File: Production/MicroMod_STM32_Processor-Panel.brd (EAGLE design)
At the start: 132.1 x 83.1 mm, 426 parts, among them J1 MICROMOD-2222, J10 MICROMOD-2222, J2 MICROMOD-2222, J3 MICROMOD-2222, J4 MICROMOD-2222, J5 MICROMOD-2222, J6 MICROMOD-2222, J7 MICROMOD-2222, J8 MICROMOD-2222, J9 MICROMOD-2222, U1 STM32F405RGT6, U10 W25QXX128MBIT-6X5, U11 STM32F405RGT6, U12 W25QXX128MBIT-6X5, U13 STM32F405RGT6, U14 W25QXX128MBIT-6X5, U15 STM32F405RGT6, U16 W25QXX128MBIT-6X5, U17 STM32F405RGT6, U18 W25QXX128MBIT-6X5, U19 STM32F405RGT6, U2 STM32F405RGT6, U20 W25QXX128MBIT-6X5, U3 W25QXX128MBIT-6X5, U4 W25QXX128MBIT-6X5, U5 STM32F405RGT6, U6 W25QXX128MBIT-6X5, U7 STM32F405RGT6, U8 W25QXX128MBIT-6X5, U9 STM32F405RGT6, Y1 12MHz, Y10 32.768kHz, Y11 12MHz, Y12 32.768kHz, Y13 12MHz, Y14 32.768kHz, Y15 12MHz, Y16 32.768kHz, Y17 12MHz, Y18 32.768kHz, Y19 12MHz, Y2 32.768kHz, Y20 32.768kHz, Y3 12MHz, Y4 32.768kHz, Y5 12MHz, Y6 32.768kHz, Y7 12MHz, Y8 32.768kHz, Y9 12MHz

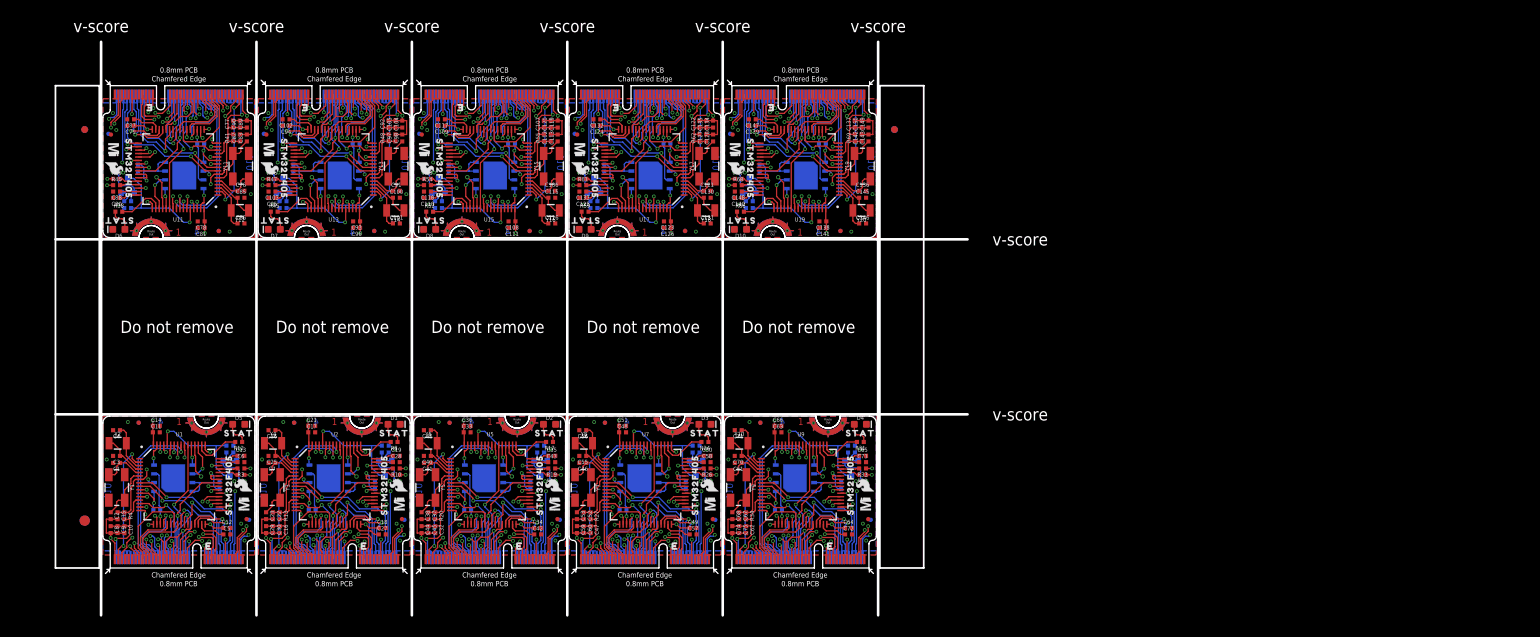
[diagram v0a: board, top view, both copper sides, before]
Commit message: Updated Panel
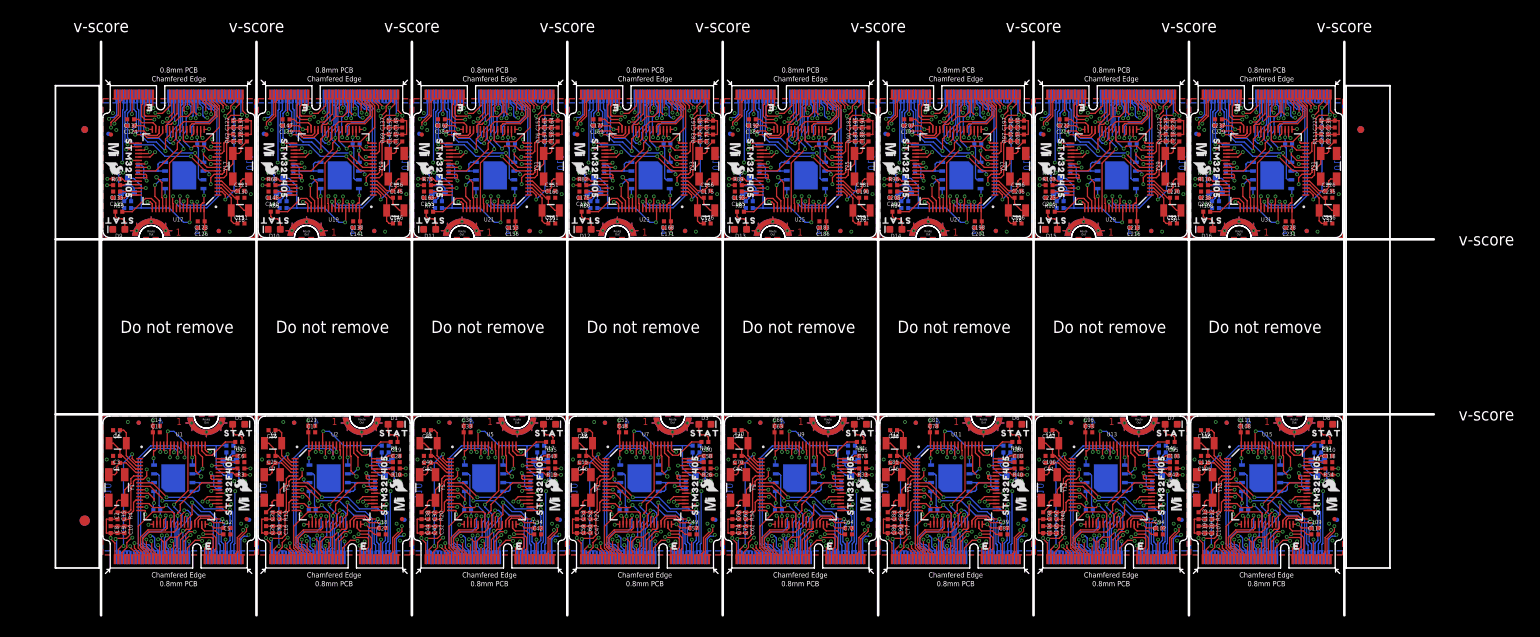
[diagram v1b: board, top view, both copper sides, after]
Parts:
- added C151, C158, C166, C173, C181, C188, C196, C203, C211, C218, C226, C233: 22pF, SparkFun-Capacitors:0402-TIGHT
- added C152, C167, C182, C197, C212, C227: 4.7uF, SparkFun-Capacitors:0402-TIGHT
- added C153, C154, C155, C156, C157, C159, C164, C168, C169, C170, C171, C172, C174, C179, C183, C184, C185, C186, C187, C189, C194, C198, C199, C200, C201, C202, C204, C209, C213, C214, C215, C216, C217, C219, C224, C228, C229, C230, C231, C232, C234, C239: 0.1uF, SparkFun-Capacitors:0402-TIGHT
- added C160, C161, C175, C176, C190, C191, C205, C206, C220, C221, C235, C236: 15pF, SparkFun-Capacitors:0402-TIGHT
- added C162, C163, C177, C178, C192, C193, C207, C208, C222, C223, C237, C238: 2.2uF, SparkFun-Capacitors:0402-TIGHT
- added C165, C180, C195, C210, C225, C240: 1.0uF, SparkFun-Capacitors:0402-TIGHT
- added D11, D12, D13, D14, D15, D16: BLUE, SparkFun-LED:LED-0603
- added FD41, FD42, FD43, FD44, FD45, FD46, FD47, FD48, FD49, FD50, FD51, FD52, FD53, FD54, FD55, FD56, FD57, FD58, FD59, FD60, FD61, FD62, FD63, FD64: FIDUCIALUFIDUCIAL, SparkFun-Aesthetics:FIDUCIAL-MICRO
- added J11, J12, J13, J14, J15, J16: MICROMOD-2222, SparkFun-MicroMod:M.2-CARD-E-22
- added LOGO21, LOGO23, LOGO25, LOGO27, LOGO29, LOGO31: OSHW-LOGOS, SparkFun-Aesthetics:OSHW-LOGO-S
- added LOGO22, LOGO24, LOGO26, LOGO28, LOGO30, LOGO32: SFE_LOGO_NAME_FLAME.1_INCH, SparkFun-Aesthetics:SFE_LOGO_NAME_FLAME_.1
- added Q11, Q12, Q13, Q14, Q15, Q16: (no value), SparkFun-DiscreteSemi:SOT23-3
- added R100, R105, R106, R107, R112, R71, R72, R77, R78, R79, R84, R85, R86, R91, R92, R93, R98, R99: 100k, SparkFun-Resistors:0402-TIGHT
- added R101, R108, R73, R80, R87, R94: 1k, SparkFun-Resistors:0402-TIGHT
- added R102, R103, R109, R110, R74, R75, R81, R82, R88, R89, R95, R96: 22, SparkFun-Resistors:0402-TIGHT
- added R104, R111, R76, R83, R90, R97: 5.1k, SparkFun-Resistors:0402-TIGHT
- added U$100, U$107, U$72, U$79, U$86, U$93: (no value), output:STM320
- added U$101, U$108, U$73, U$80, U$87, U$94: (no value), SparkFun-MicroMod:MICROMOD_MI_LOGO_.35
- added U$102, U$109, U$74, U$81, U$88, U$95: (no value), output:STM32F4050
- added U$103, U$110, U$75, U$82, U$89, U$96: (no value), SparkFun-MicroMod:MICROMOD_LOGO_.3
- added U$104, U$111, U$76, U$83, U$90, U$97: (no value), SparkFun-Aesthetics:SFE_LOGO_FLAME_.1
- added U$105, U$112, U$77, U$84, U$91, U$98: (no value), SparkFun-Aesthetics:PRODUCTION_INSTRUCTIONS
- added U$106, U$71, U$78, U$85, U$92, U$99: (no value), output:STAT0
- added U21, U23, U25, U27, U29, U31: STM32F405RGT6, STM32_Temp:TQFP64
- added U22, U24, U26, U28, U30, U32: W25QXX128MBIT-6X5, SparkFun-MicroMod:WSON-8-6X5
- added Y21, Y23, Y25, Y27, Y29, Y31: 12MHz, SparkFun-Clocks:CRYSTAL-SMD-5X3.2-4PAD
- added Y22, Y24, Y26, Y28, Y30, Y32: 32.768kHz, SparkFun-Clocks:CRYSTAL-SMD-3.2X1.5MM
- moved U$42 166.9 mm to (149.5, 49.0), turned to 0 degrees
- moved U$49 166.9 mm to (172.0, 49.0), turned to 0 degrees
- moved U$56 166.9 mm to (194.6, 49.0), turned to 0 degrees
- moved FD23 144.2 mm to (133.7, 6.97), turned to 0 degrees
- moved FD27 144.2 mm to (156.2, 6.97), turned to 0 degrees
- moved FD31 144.2 mm to (178.7, 6.97), turned to 0 degrees
- moved FD25 143.4 mm to (155.9, 7.08), turned to 0 degrees
- moved FD29 143.4 mm to (178.4, 7.08), turned to 0 degrees
- moved FD21 143.4 mm to (133.4, 7.08), turned to 0 degrees
- moved U$45 141.1 mm to (155.5, 9.23), turned to 90 degrees
- moved U$52 141.1 mm to (178.0, 9.23), turned to 90 degrees
- moved U$38 141.1 mm to (133.0, 9.23), turned to 90 degrees
- moved C87 140.0 mm to (130.5, 4.87), turned to 0 degrees
- moved C102 140.0 mm to (153.0, 4.87), turned to 0 degrees
- moved C117 140.0 mm to (175.5, 4.87), turned to 0 degrees
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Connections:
- new net !BOOT10: J11.11, Q11.1, R77.1
- new net !BOOT11: J12.11, Q12.1, R84.1
- new net !BOOT12: J13.11, Q13.1, R91.1
- new net !BOOT13: J14.11, Q14.1, R98.1
- new net !BOOT14: J15.11, Q15.1, R105.1
- new net !BOOT15: J16.11, Q16.1, R112.1
- new net !CS10: J11.55, U21.24
- new net !CS11: J12.55, U23.24
- new net !CS12: J13.55, U25.24
- new net !CS13: J14.55, U27.24
- new net !CS14: J15.55, U29.24
- new net !CS15: J16.55, U31.24
- new net !INT10: J11.16, U21.27
- new net !INT11: J12.16, U23.27
- new net !INT12: J13.16, U25.27
- new net !INT13: J14.16, U27.27
- new net !INT14: J15.16, U29.27
- new net !INT15: J16.16, U31.27
- new net !RESET10: C157.1, J11.6, R76.1, U21.7
- new net !RESET11: C172.1, J12.6, R83.1, U23.7
- new net !RESET12: C187.1, J13.6, R90.1, U25.7
- new net !RESET13: C202.1, J14.6, R97.1, U27.7
- new net !RESET14: C217.1, J15.6, R104.1, U29.7
- new net !RESET15: C232.1, J16.6, R111.1, U31.7
- new net 3.3V10: C152.1, C153.1, C154.1, C155.1, C156.1, C159.1, C164.1, C165.1, J11.2, J11.74, Q11.2, R72.2, R76.2, R77.2, U21.13, U21.19, U21.32, U21.42, U21.43, U21.48, U21.64, U22.3, U22.7, U22.8
- new net 3.3V11: C167.1, C168.1, C169.1, C170.1, C171.1, C174.1, C179.1, C180.1, J12.2, J12.74, Q12.2, R79.2, R83.2, R84.2, U23.13, U23.19, U23.32, U23.42, U23.43, U23.48, U23.64, U24.3, U24.7, U24.8
- new net 3.3V12: C182.1, C183.1, C184.1, C185.1, C186.1, C189.1, C194.1, C195.1, J13.2, J13.74, Q13.2, R86.2, R90.2, R91.2, U25.13, U25.19, U25.32, U25.42, U25.43, U25.48, U25.64, U26.3, U26.7, U26.8
- new net 3.3V13: C197.1, C198.1, C199.1, C200.1, C201.1, C204.1, C209.1, C210.1, J14.2, J14.74, Q14.2, R93.2, R97.2, R98.2, U27.13, U27.19, U27.32, U27.42, U27.43, U27.48, U27.64, U28.3, U28.7, U28.8
- new net 3.3V14: C212.1, C213.1, C214.1, C215.1, C216.1, C219.1, C224.1, C225.1, J15.2, J15.74, Q15.2, R100.2, R104.2, R105.2, U29.13, U29.19, U29.32, U29.42, U29.43, U29.48, U29.64, U30.3, U30.7, U30.8
- new net 3.3V15: C227.1, C228.1, C229.1, C230.1, C231.1, C234.1, C239.1, C240.1, J16.2, J16.74, Q16.2, R107.2, R111.2, R112.2, U31.13, U31.19, U31.32, U31.42, U31.43, U31.48, U31.64, U32.3, U32.7, U32.8
- new net A20: J11.34, U21.25
- new net A21: J11.38, U21.26
- new net A22: J12.34, U23.25
- new net A23: J12.38, U23.26
- new net A24: J13.34, U25.25
- new net A25: J13.38, U25.26
- new net A26: J14.34, U27.25
- new net A27: J14.38, U27.26
- new net A28: J15.34, U29.25
- new net A29: J15.38, U29.26
- new net A30: J16.34, U31.25
- new net A31: J16.38, U31.26
- new net AUD_BCLK10: J11.50, U21.55
- new net AUD_BCLK11: J12.50, U23.55
- new net AUD_BCLK12: J13.50, U25.55
- new net AUD_BCLK13: J14.50, U27.55
- new net AUD_BCLK14: J15.50, U29.55
- new net AUD_BCLK15: J16.50, U31.55
- new net AUD_IN10: J11.54, U21.57
- new net AUD_IN11: J12.54, U23.57
- new net AUD_IN12: J13.54, U25.57
- new net AUD_IN13: J14.54, U27.57
- new net AUD_IN14: J15.54, U29.57
- new net AUD_IN15: J16.54, U31.57
- new net AUD_LRCLK10: J11.52, U21.20
- new net AUD_LRCLK11: J12.52, U23.20
- new net AUD_LRCLK12: J13.52, U25.20
- new net AUD_LRCLK13: J14.52, U27.20
- new net AUD_LRCLK14: J15.52, U29.20
- new net AUD_LRCLK15: J16.52, U31.20
- new net AUD_OUT10: J11.56, U21.56
- new net AUD_OUT11: J12.56, U23.56
- new net AUD_OUT12: J13.56, U25.56
- new net AUD_OUT13: J14.56, U27.56
- new net AUD_OUT14: J15.56, U29.56
- new net AUD_OUT15: J16.56, U31.56
- new net BATT_VIN10: J11.49, U21.15
- new net BATT_VIN11: J12.49, U23.15
- new net BATT_VIN12: J13.49, U25.15
- new net BATT_VIN13: J14.49, U27.15
- new net BATT_VIN14: J15.49, U29.15
- new net BATT_VIN15: J16.49, U31.15
- new net BOOT10: Q11.3, R71.2, U21.60
- new net BOOT11: Q12.3, R78.2, U23.60
- new net BOOT12: Q13.3, R85.2, U25.60
- new net BOOT13: Q14.3, R92.2, U27.60
- new net BOOT14: Q15.3, R99.2, U29.60
- new net BOOT15: Q16.3, R106.2, U31.60
- new net CAN_RX10: J11.41, U21.61
- new net CAN_RX11: J12.41, U23.61
- new net CAN_RX12: J13.41, U25.61
- new net CAN_RX13: J14.41, U27.61
- new net CAN_RX14: J15.41, U29.61
- new net CAN_RX15: J16.41, U31.61
- new net CAN_TX10: J11.43, U21.62
- new net CAN_TX11: J12.43, U23.62
- new net CAN_TX12: J13.43, U25.62
- new net CAN_TX13: J14.43, U27.62
- new net CAN_TX14: J15.43, U29.62
- new net CAN_TX15: J16.43, U31.62
- new net CIPO10: J11.61, U21.22
- new net CIPO11: J12.61, U23.22
- new net CIPO12: J13.61, U25.22
- new net CIPO13: J14.61, U27.22
- new net CIPO14: J15.61, U29.22
- new net CIPO15: J16.61, U31.22
- new net COPI10: J11.59, U21.23
- new net COPI11: J12.59, U23.23
- new net COPI12: J13.59, U25.23
- new net COPI13: J14.59, U27.23
- new net COPI14: J15.59, U29.23
- new net COPI15: J16.59, U31.23
- new net D+10: J11.3, R75.1
- new net D+11: J12.3, R82.1
- new net D+12: J13.3, R89.1
- new net D+13: J14.3, R96.1
- new net D+14: J15.3, R103.1
- new net D+15: J16.3, R110.1
- new net D-10: J11.5, R74.1
- new net D-11: J12.5, R81.1
- new net D-12: J13.5, R88.1
- new net D-13: J14.5, R95.1
- new net D-14: J15.5, R102.1
- new net D-15: J16.5, R109.1
- new net D20: J11.10, U21.8
- new net D21: J11.18, U21.9
- new net D22: J12.10, U23.8
- new net D23: J12.18, U23.9
- new net D24: J13.10, U25.8
- new net D25: J13.18, U25.9
- new net D26: J14.10, U27.8
- new net D27: J14.18, U27.9
- new net D28: J15.10, U29.8
- new net D29: J15.18, U29.9
- new net D30: J16.10, U31.8
- new net D31: J16.18, U31.9
- new net FLASH_!CS10: R72.1, U21.11, U22.1
- new net FLASH_!CS11: R79.1, U23.11, U24.1
- new net FLASH_!CS12: R86.1, U25.11, U26.1
- new net FLASH_!CS13: R93.1, U27.11, U28.1
- new net FLASH_!CS14: R100.1, U29.11, U30.1
- new net FLASH_!CS15: R107.1, U31.11, U32.1
- new net FLASH_SCK10: U21.51, U22.6
- new net FLASH_SCK11: U23.51, U24.6
- new net FLASH_SCK12: U25.51, U26.6
- new net FLASH_SCK13: U27.51, U28.6
- new net FLASH_SCK14: U29.51, U30.6
- new net FLASH_SCK15: U31.51, U32.6
- new net FLASH_SDI10: U21.53, U22.5
- new net FLASH_SDI11: U23.53, U24.5
- new net FLASH_SDI12: U25.53, U26.5
- new net FLASH_SDI13: U27.53, U28.5
- new net FLASH_SDI14: U29.53, U30.5
- new net FLASH_SDI15: U31.53, U32.5
- new net FLASH_SDO10: U21.52, U22.2
- new net FLASH_SDO11: U23.52, U24.2
- new net FLASH_SDO12: U25.52, U26.2
- new net FLASH_SDO13: U27.52, U28.2
- new net FLASH_SDO14: U29.52, U30.2
- new net FLASH_SDO15: U31.52, U32.2
- new net G100: J15.46, U29.39
- new net G101: J15.48, U29.40
- new net G102: J15.40, U29.54
- new net G103: J15.42, U29.41
- new net G104: J15.44, U29.14
- new net G105: J16.73, U31.2
- new net G106: J16.71, U31.10
- new net G107: J16.46, U31.39
- new net G108: J16.48, U31.40
- new net G109: J16.40, U31.54
- new net G110: J16.42, U31.41
- new net G111: J16.44, U31.14
- new net G70: J11.73, U21.2
- new net G71: J11.71, U21.10
- new net G72: J11.46, U21.39
- new net G73: J11.48, U21.40
- new net G74: J11.40, U21.54
- new net G75: J11.42, U21.41
- new net G76: J11.44, U21.14
- new net G77: J12.73, U23.2
- new net G78: J12.71, U23.10
- new net G79: J12.46, U23.39
- new net G80: J12.48, U23.40
- new net G81: J12.40, U23.54
- new net G82: J12.42, U23.41
- new net G83: J12.44, U23.14
- new net G84: J13.73, U25.2
- new net G85: J13.71, U25.10
- new net G86: J13.46, U25.39
- new net G87: J13.48, U25.40
- new net G88: J13.40, U25.54
- new net G89: J13.42, U25.41
- new net G90: J13.44, U25.14
- new net G91: J14.73, U27.2
- new net G92: J14.71, U27.10
- new net G93: J14.46, U27.39
- new net G94: J14.48, U27.40
- new net G95: J14.40, U27.54
- new net G96: J14.42, U27.41
- new net G97: J14.44, U27.14
- new net G98: J15.73, U29.2
- new net G99: J15.71, U29.10
- new net GND10: C151.2, C152.2, C153.2, C154.2, C155.2, C156.2, C157.2, C158.2, C159.2, C160.2, C161.2, C162.2, C163.2, C164.2, C165.2, D11.C, J11.1, J11.33, J11.36, J11.39, J11.45, J11.7, J11.75, J11.GND1, J11.GND2, J11.GND3, R71.1, U21.12, U21.18, U21.28, U21.63, U22.4
- new net GND11: C166.2, C167.2, C168.2, C169.2, C170.2, C171.2, C172.2, C173.2, C174.2, C175.2, C176.2, C177.2, C178.2, C179.2, C180.2, D12.C, J12.1, J12.33, J12.36, J12.39, J12.45, J12.7, J12.75, J12.GND1, J12.GND2, J12.GND3, R78.1, U23.12, U23.18, U23.28, U23.63, U24.4
- new net GND12: C181.2, C182.2, C183.2, C184.2, C185.2, C186.2, C187.2, C188.2, C189.2, C190.2, C191.2, C192.2, C193.2, C194.2, C195.2, D13.C, J13.1, J13.33, J13.36, J13.39, J13.45, J13.7, J13.75, J13.GND1, J13.GND2, J13.GND3, R85.1, U25.12, U25.18, U25.28, U25.63, U26.4
- new net GND13: C196.2, C197.2, C198.2, C199.2, C200.2, C201.2, C202.2, C203.2, C204.2, C205.2, C206.2, C207.2, C208.2, C209.2, C210.2, D14.C, J14.1, J14.33, J14.36, J14.39, J14.45, J14.7, J14.75, J14.GND1, J14.GND2, J14.GND3, R92.1, U27.12, U27.18, U27.28, U27.63, U28.4
- new net GND14: C211.2, C212.2, C213.2, C214.2, C215.2, C216.2, C217.2, C218.2, C219.2, C220.2, C221.2, C222.2, C223.2, C224.2, C225.2, D15.C, J15.1, J15.33, J15.36, J15.39, J15.45, J15.7, J15.75, J15.GND1, J15.GND2, J15.GND3, R99.1, U29.12, U29.18, U29.28, U29.63, U30.4
- new net GND15: C226.2, C227.2, C228.2, C229.2, C230.2, C231.2, C232.2, C233.2, C234.2, C235.2, C236.2, C237.2, C238.2, C239.2, C240.2, D16.C, J16.1, J16.33, J16.36, J16.39, J16.45, J16.7, J16.75, J16.GND1, J16.GND2, J16.GND3, R106.1, U31.12, U31.18, U31.28, U31.63, U32.4
- new net HOST_D+10: J11.35, U21.36
- new net HOST_D+11: J12.35, U23.36
- new net HOST_D+12: J13.35, U25.36
- new net HOST_D+13: J14.35, U27.36
- new net HOST_D+14: J15.35, U29.36
- new net HOST_D+15: J16.35, U31.36
- new net HOST_D-10: J11.37, U21.35
- new net HOST_D-11: J12.37, U23.35
- new net HOST_D-12: J13.37, U25.35
- new net HOST_D-13: J14.37, U27.35
- new net HOST_D-14: J15.37, U29.35
- new net HOST_D-15: J16.37, U31.35
- new net HOST_ID10: J11.8, U21.33
- new net HOST_ID11: J12.8, U23.33
- new net HOST_ID12: J13.8, U25.33
- new net HOST_ID13: J14.8, U27.33
- new net HOST_ID14: J15.8, U29.33
- new net HOST_ID15: J16.8, U31.33
- new net HOST_VBUS10: J11.63, U21.34
- new net HOST_VBUS11: J12.63, U23.34
- new net HOST_VBUS12: J13.63, U25.34
- new net HOST_VBUS13: J14.63, U27.34
- new net HOST_VBUS14: J15.63, U29.34
- new net HOST_VBUS15: J16.63, U31.34
- new net N$100: C176.1, U23.3, Y24.P$2
- new net N$101: C175.1, U23.4, Y24.P$1
- new net N$102: C173.1, U23.6, Y23.3
- new net N$103: C166.1, U23.5, Y23.1
- new net N$104: C178.1, U23.47
- new net N$105: C177.1, U23.31
- new net N$106: D12.A, R80.1
- new net N$107: R81.2, U23.44
- new net N$108: R82.2, U23.45
- new net N$109: C191.1, U25.3, Y26.P$2
- new net N$110: C190.1, U25.4, Y26.P$1
- new net N$111: C188.1, U25.6, Y25.3
- new net N$112: C181.1, U25.5, Y25.1
- new net N$113: C193.1, U25.47
- new net N$114: C192.1, U25.31
- new net N$115: D13.A, R87.1
- new net N$116: R88.2, U25.44
- new net N$117: R89.2, U25.45
- new net N$118: C206.1, U27.3, Y28.P$2
- new net N$119: C205.1, U27.4, Y28.P$1
- new net N$120: C203.1, U27.6, Y27.3
- new net N$121: C196.1, U27.5, Y27.1
- new net N$122: C208.1, U27.47
- new net N$123: C207.1, U27.31
- new net N$124: D14.A, R94.1
- new net N$125: R95.2, U27.44
- new net N$126: R96.2, U27.45
- new net N$127: C221.1, U29.3, Y30.P$2
- new net N$128: C220.1, U29.4, Y30.P$1
- new net N$129: C218.1, U29.6, Y29.3
- new net N$130: C211.1, U29.5, Y29.1
- new net N$131: C223.1, U29.47
- new net N$132: C222.1, U29.31
- new net N$133: D15.A, R101.1
- new net N$134: R102.2, U29.44
- new net N$135: R103.2, U29.45
- new net N$136: C236.1, U31.3, Y32.P$2
- new net N$137: C235.1, U31.4, Y32.P$1
- new net N$138: C233.1, U31.6, Y31.3
- new net N$139: C226.1, U31.5, Y31.1
- new net N$140: C238.1, U31.47
- new net N$141: C237.1, U31.31
- new net N$142: D16.A, R108.1
- new net N$143: R109.2, U31.44
- new net N$144: R110.2, U31.45
- new net N$91: C161.1, U21.3, Y22.P$2
- new net N$92: C160.1, U21.4, Y22.P$1
- new net N$93: C158.1, U21.6, Y21.3
- new net N$94: C151.1, U21.5, Y21.1
- new net N$95: C163.1, U21.47
- new net N$96: C162.1, U21.31
- new net N$97: D11.A, R73.1
- new net N$98: R74.2, U21.44
- new net N$99: R75.2, U21.45
- new net PWM20: J11.32, U21.37
- new net PWM21: J11.47, U21.38
- new net PWM22: J12.32, U23.37
- new net PWM23: J12.47, U23.38
- new net PWM24: J13.32, U25.37
- new net PWM25: J13.47, U25.38
- new net PWM26: J14.32, U27.37
- new net PWM27: J14.47, U27.38
- new net PWM28: J15.32, U29.37
- new net PWM29: J15.47, U29.38
- new net PWM30: J16.32, U31.37
- new net PWM31: J16.47, U31.38
- new net RX11: J11.19, U21.17
- new net RX12: J12.19, U23.17
- new net RX13: J13.19, U25.17
- new net RX14: J14.19, U27.17
- new net RX15: J15.19, U29.17
- new net RX16: J16.19, U31.17
- new net SCK10: J11.57, U21.21
- new net SCK11: J12.57, U23.21
- new net SCK12: J13.57, U25.21
- new net SCK13: J14.57, U27.21
- new net SCK14: J15.57, U29.21
- new net SCK15: J16.57, U31.21
- new net SCL20: J11.14, U21.29
- new net SCL21: J11.53, U21.58
- new net SCL22: J12.14, U23.29
- new net SCL23: J12.53, U23.58
- new net SCL24: J13.14, U25.29
- new net SCL25: J13.53, U25.58
- new net SCL26: J14.14, U27.29
- new net SCL27: J14.53, U27.58
- new net SCL28: J15.14, U29.29
- new net SCL29: J15.53, U29.58
- new net SCL30: J16.14, U31.29
- new net SCL31: J16.53, U31.58
- new net SDA20: J11.12, U21.30
- new net SDA21: J11.51, U21.59
- new net SDA22: J12.12, U23.30
- new net SDA23: J12.51, U23.59
- new net SDA24: J13.12, U25.30
- new net SDA25: J13.51, U25.59
- new net SDA26: J14.12, U27.30
- new net SDA27: J14.51, U27.59
- new net SDA28: J15.12, U29.30
- new net SDA29: J15.51, U29.59
- new net SDA30: J16.12, U31.30
- new net SDA31: J16.51, U31.59
- new net STAT10: R73.2, U21.50
- new net STAT11: R80.2, U23.50
- new net STAT12: R87.2, U25.50
- new net STAT13: R94.2, U27.50
- new net STAT14: R101.2, U29.50
- new net STAT15: R108.2, U31.50
- new net SWCLK10: J11.21, U21.49
- new net SWCLK11: J12.21, U23.49
- new net SWCLK12: J13.21, U25.49
- new net SWCLK13: J14.21, U27.49
- new net SWCLK14: J15.21, U29.49
- new net SWCLK15: J16.21, U31.49
- new net SWDIO10: J11.23, U21.46
- new net SWDIO11: J12.23, U23.46
- new net SWDIO12: J13.23, U25.46
- new net SWDIO13: J14.23, U27.46
- new net SWDIO14: J15.23, U29.46
- new net SWDIO15: J16.23, U31.46
- new net TX11: J11.17, U21.16
- new net TX12: J12.17, U23.16
- new net TX13: J13.17, U25.16
- new net TX14: J14.17, U27.16
- new net TX15: J15.17, U29.16
- new net TX16: J16.17, U31.16
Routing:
- net 3.3V14: track 0.00 -> 49.7 mm, vias 0 -> 7
- net 3.3V12: track 0.00 -> 49.7 mm, vias 0 -> 7
- net 3.3V11: track 0.00 -> 49.7 mm, vias 0 -> 7
- net 3.3V10: track 0.00 -> 49.7 mm, vias 0 -> 7
- net 3.3V15: track 0.00 -> 49.7 mm, vias 0 -> 7
- net 3.3V13: track 0.00 -> 49.7 mm, vias 0 -> 7
- net HOST_VBUS12: track 0.00 -> 42.0 mm, vias 0 -> 2
- net HOST_VBUS11: track 0.00 -> 42.0 mm, vias 0 -> 2
- net HOST_VBUS10: track 0.00 -> 42.0 mm, vias 0 -> 2
- net HOST_VBUS13: track 0.00 -> 42.0 mm, vias 0 -> 2
- net HOST_VBUS15: track 0.00 -> 42.0 mm, vias 0 -> 2
- net HOST_VBUS14: track 0.00 -> 42.0 mm, vias 0 -> 2
- net !RESET10: track 0.00 -> 35.5 mm, vias 0 -> 2
- net !RESET15: track 0.00 -> 35.5 mm, vias 0 -> 2
- net !RESET14: track 0.00 -> 35.5 mm, vias 0 -> 2
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- added copper zone on layer 15, net 3.3V10
- added copper zone on layer 15, net 3.3V11
- added copper zone on layer 15, net 3.3V12
- added copper zone on layer 15, net 3.3V13
- added copper zone on layer 15, net 3.3V14
- added copper zone on layer 15, net 3.3V15
- added copper zone on layer 1, net GND10
- added copper zone on layer 16, net GND10
- added copper zone on layer 2, net GND10
- added copper zone on layer 1, net GND11
- added copper zone on layer 16, net GND11
- added copper zone on layer 2, net GND11
- added copper zone on layer 1, net GND12
- added copper zone on layer 16, net GND12
- added copper zone on layer 2, net GND12
- added copper zone on layer 1, net GND13
- added copper zone on layer 16, net GND13
- added copper zone on layer 2, net GND13
- added copper zone on layer 1, net GND14
- added copper zone on layer 16, net GND14
- added copper zone on layer 2, net GND14
- added copper zone on layer 1, net GND15
- added copper zone on layer 16, net GND15
- added copper zone on layer 2, net GND15
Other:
- board size 132.1 x 83.1 mm -> 199.6 x 83.1 mm

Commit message: Update for v20 pushing to reds.
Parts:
- removed U$100, U$107: (no value), output:STM320
- removed U$101, U$108: (no value), SparkFun-MicroMod:MICROMOD_MI_LOGO_.35
- removed U$102, U$109: (no value), output:STM32F4050
- removed U$103, U$110: (no value), SparkFun-MicroMod:MICROMOD_LOGO_.3
- removed U$104, U$111, U$97: (no value), SparkFun-Aesthetics:SFE_LOGO_FLAME_.1
- removed U$105, U$112, U$98: (no value), SparkFun-Aesthetics:PRODUCTION_INSTRUCTIONS
- removed U$106, U$99: (no value), output:STAT0
- U$10, U$52, U$94: device SparkFun-MicroMod:MICROMOD_MI_LOGO_.35 -> output:STM32F4050
- U$11, U$53, U$95: device output:STM32F4050 -> SparkFun-MicroMod:MICROMOD_LOGO_.3
- U$12, U$54, U$96: device SparkFun-MicroMod:MICROMOD_LOGO_.3 -> SparkFun-Aesthetics:SFE_LOGO_FLAME_.1
- U$13, U$55: device SparkFun-Aesthetics:SFE_LOGO_FLAME_.1 -> output:STAT0
- U$14, U$56: device SparkFun-Aesthetics:PRODUCTION_INSTRUCTIONS -> output:STM320
- U$15, U$57: device output:STAT0 -> SparkFun-MicroMod:MICROMOD_MI_LOGO_.35
- U$16, U$58: device output:STM320 -> output:STM32F4050
- U$17, U$59: device SparkFun-MicroMod:MICROMOD_MI_LOGO_.35 -> SparkFun-MicroMod:MICROMOD_LOGO_.3
- U$18, U$60: device output:STM32F4050 -> SparkFun-Aesthetics:SFE_LOGO_FLAME_.1
- U$19, U$61: device SparkFun-MicroMod:MICROMOD_LOGO_.3 -> output:STAT0
- U$20, U$62: device SparkFun-Aesthetics:SFE_LOGO_FLAME_.1 -> output:STM320
- U$21, U$63: device SparkFun-Aesthetics:PRODUCTION_INSTRUCTIONS -> SparkFun-MicroMod:MICROMOD_MI_LOGO_.35
- U$22, U$64: device output:STAT0 -> output:STM32F4050
- U$23, U$65: device output:STM320 -> SparkFun-MicroMod:MICROMOD_LOGO_.3
- U$24, U$66: device SparkFun-MicroMod:MICROMOD_MI_LOGO_.35 -> SparkFun-Aesthetics:SFE_LOGO_FLAME_.1
- U$25, U$67: device output:STM32F4050 -> output:STAT0
- U$26, U$68: device SparkFun-MicroMod:MICROMOD_LOGO_.3 -> output:STM320
- U$27, U$69: device SparkFun-Aesthetics:SFE_LOGO_FLAME_.1 -> SparkFun-MicroMod:MICROMOD_MI_LOGO_.35
- U$28, U$70: device SparkFun-Aesthetics:PRODUCTION_INSTRUCTIONS -> output:STM32F4050
- U$29, U$71: device output:STAT0 -> SparkFun-MicroMod:MICROMOD_LOGO_.3
- U$30, U$72: device output:STM320 -> SparkFun-Aesthetics:SFE_LOGO_FLAME_.1
- U$31, U$73: device SparkFun-MicroMod:MICROMOD_MI_LOGO_.35 -> output:STAT0
- U$32, U$74: device output:STM32F4050 -> output:STM320
- U$33, U$75: device SparkFun-MicroMod:MICROMOD_LOGO_.3 -> SparkFun-MicroMod:MICROMOD_MI_LOGO_.35
- U$34, U$76: device SparkFun-Aesthetics:SFE_LOGO_FLAME_.1 -> output:STM32F4050
- U$35, U$77: device SparkFun-Aesthetics:PRODUCTION_INSTRUCTIONS -> SparkFun-MicroMod:MICROMOD_LOGO_.3
- U$36, U$78: device output:STAT0 -> SparkFun-Aesthetics:SFE_LOGO_FLAME_.1
- U$37, U$79: device output:STM320 -> output:STAT0
- U$38, U$80: device SparkFun-MicroMod:MICROMOD_MI_LOGO_.35 -> output:STM320
- U$39, U$81: device output:STM32F4050 -> SparkFun-MicroMod:MICROMOD_MI_LOGO_.35
- U$40, U$82: device SparkFun-MicroMod:MICROMOD_LOGO_.3 -> output:STM32F4050
- U$41, U$83: device SparkFun-Aesthetics:SFE_LOGO_FLAME_.1 -> SparkFun-MicroMod:MICROMOD_LOGO_.3
- U$42, U$84: device SparkFun-Aesthetics:PRODUCTION_INSTRUCTIONS -> SparkFun-Aesthetics:SFE_LOGO_FLAME_.1
- U$49, U$7, U$91: device SparkFun-Aesthetics:PRODUCTION_INSTRUCTIONS -> output:STAT0
- U$50, U$8, U$92: device output:STAT0 -> output:STM320
- U$51, U$9, U$93: device output:STM320 -> SparkFun-MicroMod:MICROMOD_MI_LOGO_.35
- U1, U11, U13, U15, U17, U19, U2, U21, U23, U25, U27, U29, U31, U5, U7, U9: device STM32_Temp:TQFP64 -> SparkFun-IC-Microcontroller:TQFP64
- moved U$52 180.9 mm to (3.74, 57.9), turned to 270 degrees
- moved U$51 176.9 mm to (1.38, 60.6), flipped to the top, turned to 270 degrees
- moved U$50 173.1 mm to (9.84, 63.5), flipped to the bottom, turned to 180 degrees
- moved U$49 169.7 mm to (2.32, 50.3), turned to 180 degrees
- moved U$54 169.1 mm to (1.68, 57.9), flipped to the top, turned to 270 degrees
- moved U$53 167.1 mm to (16.8, 63.5), flipped to the bottom, turned to 180 degrees
- moved U$56 162.9 mm to (32.3, 63.5), flipped to the bottom, turned to 180 degrees
- moved U$55 157.8 mm to (24.8, 50.3), turned to 180 degrees
- moved U$91 89.8 mm to (159.9, 50.3)
- moved U$77 87.9 mm to (106.9, 63.5), flipped to the bottom
- moved U$70 73.7 mm to (71.3, 57.9), turned to 270 degrees
- moved U$63 73.2 mm to (46.4, 60.6), turned to 270 degrees
- moved U$84 72.0 mm to (114.2, 57.9), turned to 270 degrees
- moved U$83 60.4 mm to (129.4, 63.5), flipped to the bottom, turned to 180 degrees
- moved U$95 58.4 mm to (174.4, 63.5), flipped to the bottom, turned to 180 degrees
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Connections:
- net CIPO renamed POCI
- net CIPO1 renamed POCI1
- net CIPO10 renamed POCI10
- net CIPO11 renamed POCI11
- net CIPO12 renamed POCI12
- net CIPO13 renamed POCI13
- net CIPO14 renamed POCI14
- net CIPO15 renamed POCI15
- net CIPO2 renamed POCI2
- net CIPO3 renamed POCI3
- net CIPO4 renamed POCI4
- net CIPO5 renamed POCI5
- net CIPO6 renamed POCI6
- net CIPO7 renamed POCI7
- net CIPO8 renamed POCI8
- net CIPO9 renamed POCI9
- net COPI renamed PICO
- net COPI1 renamed PICO1
- net COPI10 renamed PICO10
- net COPI11 renamed PICO11
- net COPI12 renamed PICO12
- net COPI13 renamed PICO13
- net COPI14 renamed PICO14
- net COPI15 renamed PICO15
- net COPI2 renamed PICO2
- net COPI3 renamed PICO3
- net COPI4 renamed PICO4
- net COPI5 renamed PICO5
- net COPI6 renamed PICO6
- net COPI7 renamed PICO7
- net COPI8 renamed PICO8
- net COPI9 renamed PICO9
- net 3.3V: no longer U1.42, U1.43
- net 3.3V1: no longer U2.42, U2.43
- net 3.3V10: no longer U21.42, U21.43
- net 3.3V11: no longer U23.42, U23.43
- net 3.3V12: no longer U25.42, U25.43
- net 3.3V13: no longer U27.42, U27.43
- net 3.3V14: no longer U29.42, U29.43
- net 3.3V15: no longer U31.42, U31.43
- net 3.3V2: no longer U5.42, U5.43
- net 3.3V3: no longer U7.42, U7.43
- net 3.3V4: no longer U9.42, U9.43
- net 3.3V5: no longer U11.42, U11.43
- net 3.3V6: no longer U13.42, U13.43
- net 3.3V7: no longer U15.42, U15.43
- net 3.3V8: no longer U17.42, U17.43
- net 3.3V9: no longer U19.42, U19.43
- net GND: now also U1.16, U1.17
- net GND1: now also U2.16, U2.17
- net GND10: now also U21.16, U21.17
- net GND11: now also U23.16, U23.17
- net GND12: now also U25.16, U25.17
- net GND13: now also U27.16, U27.17
- net GND14: now also U29.16, U29.17
- net GND15: now also U31.16, U31.17
- net GND2: now also U5.16, U5.17
- net GND3: now also U7.16, U7.17
- net GND4: now also U9.16, U9.17
- net GND5: now also U11.16, U11.17
- net GND6: now also U13.16, U13.17
- net GND7: now also U15.16, U15.17
- net GND8: now also U17.16, U17.17
- net GND9: now also U19.16, U19.17
- net RX1: now also U1.43; no longer U1.17
- net RX10: now also U19.43; no longer U19.17
- net RX11: now also U21.43; no longer U21.17
- net RX12: now also U23.43; no longer U23.17
- net RX13: now also U25.43; no longer U25.17
- net RX14: now also U27.43; no longer U27.17
- net RX15: now also U29.43; no longer U29.17
- net RX16: now also U31.43; no longer U31.17
- net RX2: now also U2.43; no longer U2.17
- net RX3: now also U5.43; no longer U5.17
- net RX4: now also U7.43; no longer U7.17
- net RX5: now also U9.43; no longer U9.17
- net RX6: now also U11.43; no longer U11.17
- net RX7: now also U13.43; no longer U13.17
- net RX8: now also U15.43; no longer U15.17
- net RX9: now also U17.43; no longer U17.17
- net TX1: now also U1.42; no longer U1.16
- net TX10: now also U19.42; no longer U19.16
- net TX11: now also U21.42; no longer U21.16
- net TX12: now also U23.42; no longer U23.16
- net TX13: now also U25.42; no longer U25.16
- net TX14: now also U27.42; no longer U27.16
- net TX15: now also U29.42; no longer U29.16
- net TX16: now also U31.42; no longer U31.16
- net TX2: now also U2.42; no longer U2.16
- net TX3: now also U5.42; no longer U5.16
- net TX4: now also U7.42; no longer U7.16
- net TX5: now also U9.42; no longer U9.16
- net TX6: now also U11.42; no longer U11.16
- net TX7: now also U13.42; no longer U13.16
- net TX8: now also U15.42; no longer U15.16
- net TX9: now also U17.42; no longer U17.16
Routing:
- net TX14: track 16.6 -> 14.8 mm
- net TX12: track 16.6 -> 14.8 mm
- net TX9: track 16.6 -> 14.8 mm
- net TX13: track 16.6 -> 14.8 mm
- net TX10: track 16.6 -> 14.8 mm
- net TX16: track 16.6 -> 14.8 mm
- net TX11: track 16.6 -> 14.8 mm
- net TX5: track 16.6 -> 14.8 mm
- net TX15: track 16.6 -> 14.8 mm
- net TX2: track 16.6 -> 14.8 mm
- net TX1: track 16.6 -> 14.8 mm
- net TX8: track 16.6 -> 14.8 mm
- net TX7: track 16.6 -> 14.8 mm
- net TX3: track 16.6 -> 14.8 mm
- net TX6: track 16.6 -> 14.8 mm
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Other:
- board size 199.6 x 83.1 mm -> 203.2 x 84.1 mm
- board text added: "v20"
- board text removed: "v10"
